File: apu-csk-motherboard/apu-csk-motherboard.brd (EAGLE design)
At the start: 90.2 x 95.9 mm, 19 parts, among them U1 DS3231M+TRL

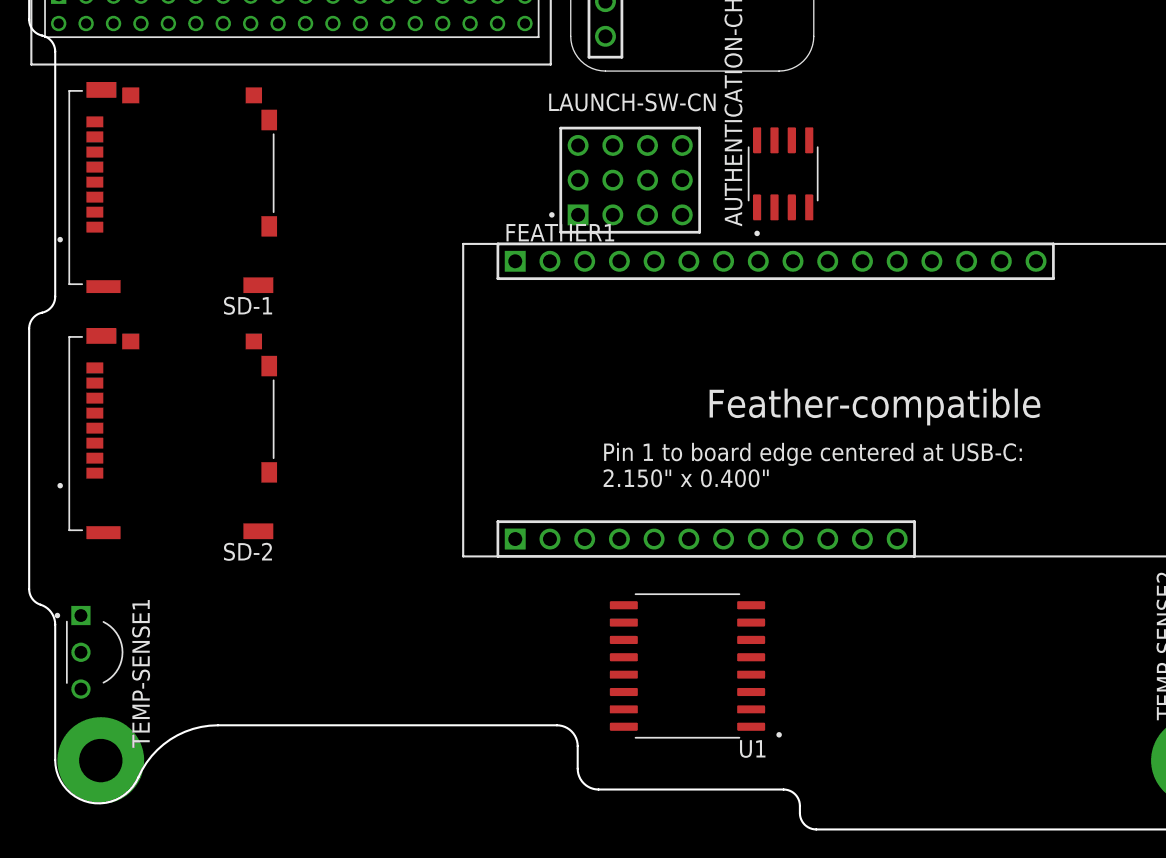
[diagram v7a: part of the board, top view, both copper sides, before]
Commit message: Just need to add capacitors
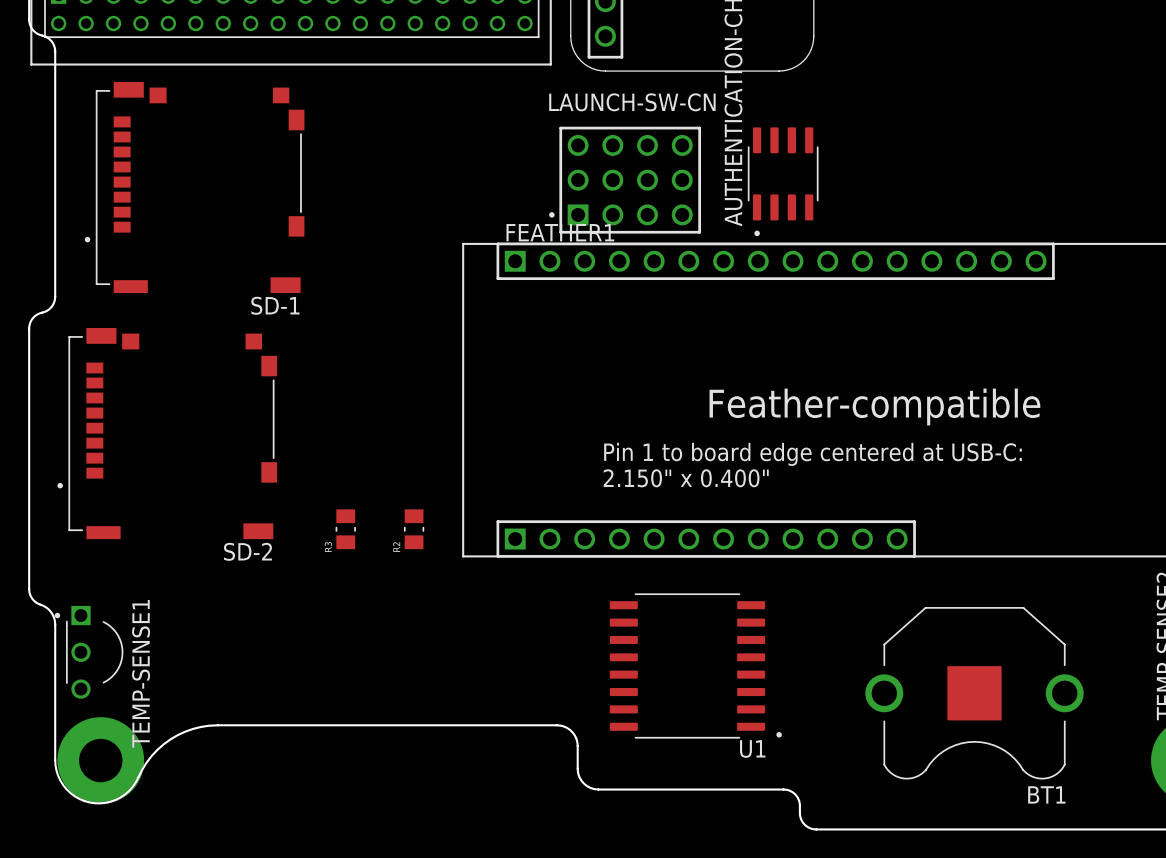
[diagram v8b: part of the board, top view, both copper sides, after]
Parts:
- added BT1: BK-890, apu-csk-motherboard:BAT_BK-890
- added R2, R3: RMCF0805JT10K0, RMCF0805JT10K0:RESC2012X65N
- AUTHENTICATION-CHIP: device ATECC608A-SSHDA-B:SOIC127P600X175-8N -> apu-csk-motherboard:SOIC127P600X175-8N
- SD-1, SD-2: device 503182-1852:MOLEX_503182-1852 -> apu-csk-motherboard:MOLEX_503182-1852
- TEMP-SENSE1, TEMP-SENSE2, TEMP-SENSE3, TEMP-SENSE4: device DS18B20:TO92269P495H695-3 -> apu-csk-motherboard:TO92269P495H695-3
- U1: device DS3231M_TRL:SOIC127P1032X265-16N -> apu-csk-motherboard:SOIC127P1032X265-16N
- moved SD-1 2.00 mm to (13.0, 47.0)
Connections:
- removed net 5V: PL3.1
- removed net CS-SD: H1.24
- removed net N$11: U1.3
- removed net N$2: H1.22
- removed net N$3: H1.20
- removed net N$4: H1.18
- removed net N$5: H1.23
- removed net N$6: U1.14
- removed net N$7: H1.19
- removed net N$8: H1.17
- removed net N$9: U1.4
- removed net RTCLOCK: U1.1
- removed net WP-FRAM: FEATHER1.B3, R1.08
- new net FE_EN: FEATHER1.B11, PL3.24
- new net FE_IO0: FEATHER1.B3, PL3.10
- new net FE_IO1: FEATHER1.B4, PL3.12
- new net FE_IO10: FEATHER1.B7, PL3.18
- new net FE_IO11: FEATHER1.B8, PL3.20
- new net FE_IO2: FEATHER1.B5, PL3.14
- new net FE_IO23: FEATHER1.T7, PL3.28
- new net FE_IO9: FEATHER1.B6, PL3.16
- new net FE_RESET: FEATHER1.T16, PL3.30
- new net FE_V_BATT: FEATHER1.B12, PL3.26
- new net FE_V_USB: FEATHER1.B10, PL3.22
- new net N$1: BT1.S1+, BT1.S2+, U1.14
- net 3.3V: now also R2.2, R3.2
- net GND: now also BT1.-
- net LSW-1-C: now also PL2.30
- net LSW-1-NC: now also PL2.14
- net LSW-1-NO: now also PL2.22
- net LSW-2-C: now also PL2.32
- net LSW-2-NC: now also PL2.16
- net LSW-2-NO: now also PL2.24
- net LSW-3-C: now also PL2.34
- net LSW-3-NC: now also PL2.18
- net LSW-3-NO: now also PL2.26
- net LSW-4-C: now also PL2.36
- net LSW-4-NC: now also PL2.20
- net LSW-4-NO: now also PL2.28
- net SCL: now also R3.1
- net SDA: now also R2.1
